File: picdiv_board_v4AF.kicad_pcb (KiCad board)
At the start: 2 copper layers, 75 x 100 mm, 83 parts, among them J1 DC-Input, J10 PPS_B, J11 PPS_B, J2 MountingHole_M2.5, J3 MountingHole_M2.5, J4 TEST_1PPS, J5 Conn_01x06, J8 PPS_A, J9 PPS_A, SW1 SW_DIP_x03, U1 LT1963AxST-3.3, U2 LT1963AxST-3.3, U3 PIC12F675-xSN, U4 LTC6993xS6-1, U5 IDT5PB1108, U6 IDT5PB1108, U7 LT1963AEQ, U8 ADR4540

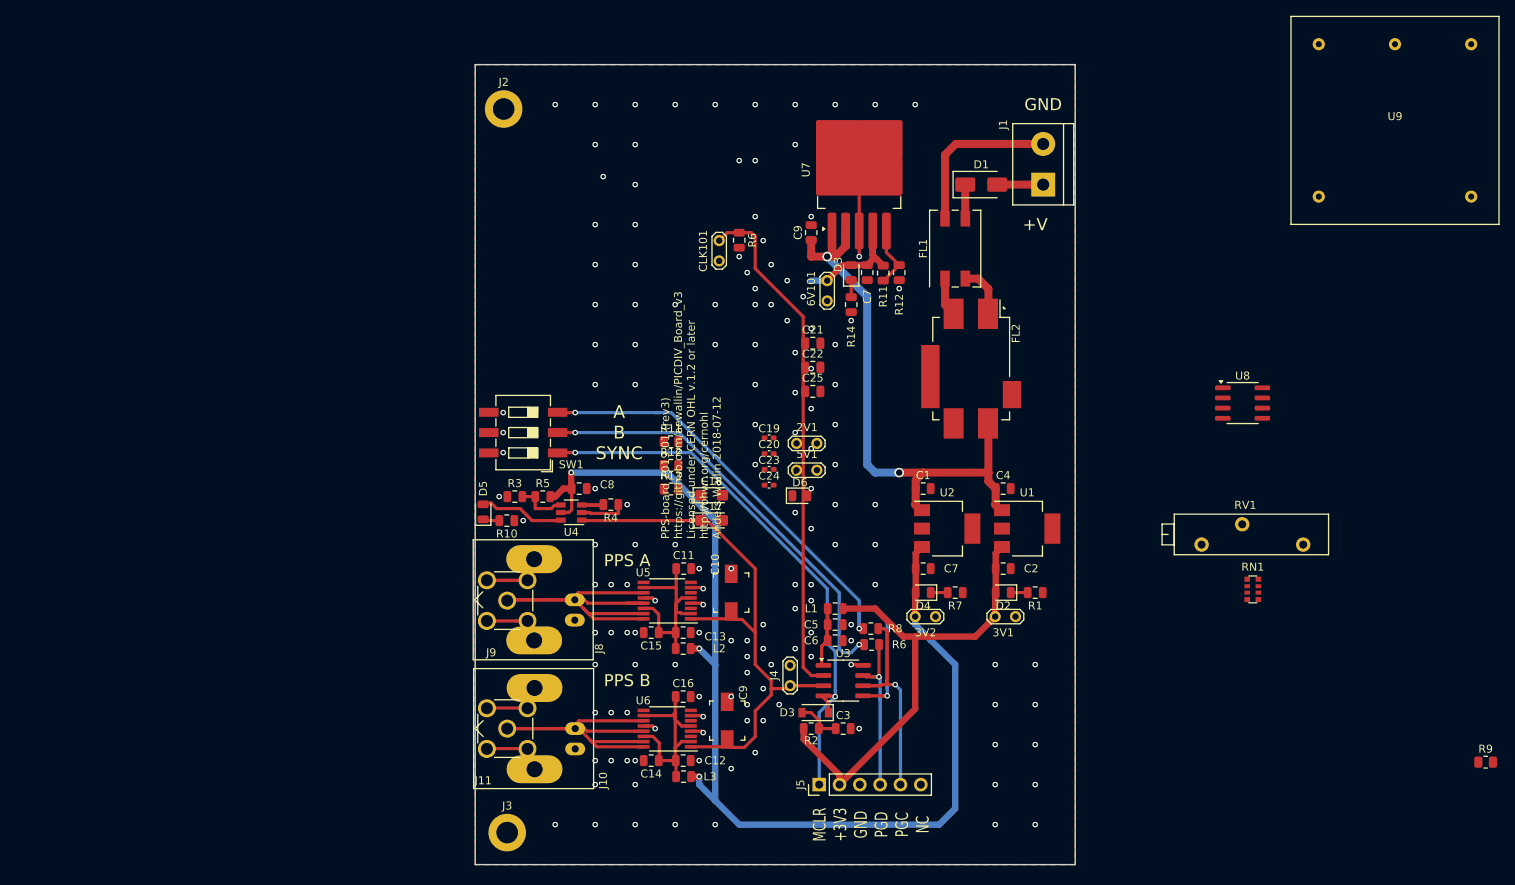
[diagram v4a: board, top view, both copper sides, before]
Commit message: Getting closer on parts placement.
Fixed a few backwards parts caused by newer libraries.  Several are mirrors of what was in the orginal symbol.  I wonder if he made his own to make the schematic clearer.
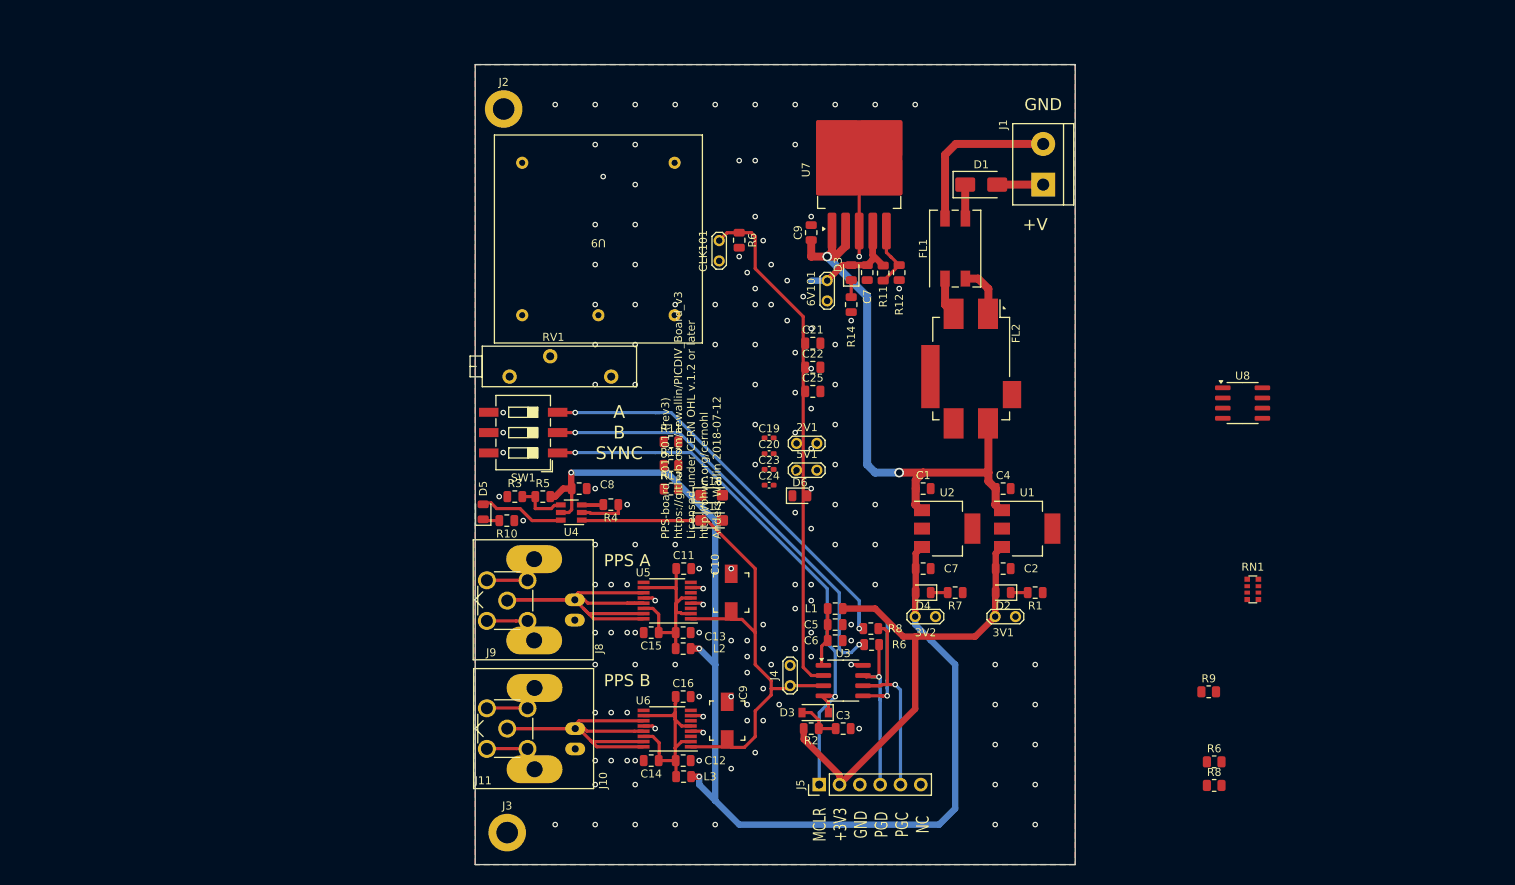
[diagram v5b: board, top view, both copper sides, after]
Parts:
- added R6: 10k, Resistor_SMD:R_0805_2012Metric, F.Cu at (217.4, 137.2)
- added R8: 10k, Resistor_SMD:R_0805_2012Metric, F.Cu at (217.4, 140.1)
- moved U9 100.7 mm to (140.4, 71.8), turned to 180 degrees
- moved RV1 89.0 mm to (142.0, 89.0)
- moved R9 35.7 mm to (216.7, 128.4)
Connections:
- U3 pad 2: /sync -> 10MHz
- U3 pad 3: PGC -> PPS
- U3 pad 4: PGD -> MCLR
- U3 pad 5: 10MHz -> /sync
- U3 pad 6: PPS -> PGC
- U3 pad 7: MCLR -> PGD
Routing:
- net 10MHz: track 13.5 -> 0.00 mm, vias 1 -> 0
- net /sync: track 0.00 -> 13.5 mm, vias 0 -> 1
- net Net-(RN1-R2.2): vias 0 -> 1
- net GND: vias 148 -> 147

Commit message: More layout work
99.5x100 mm board.
Sync back on the schematic.
Move some parts to make room for OCXO
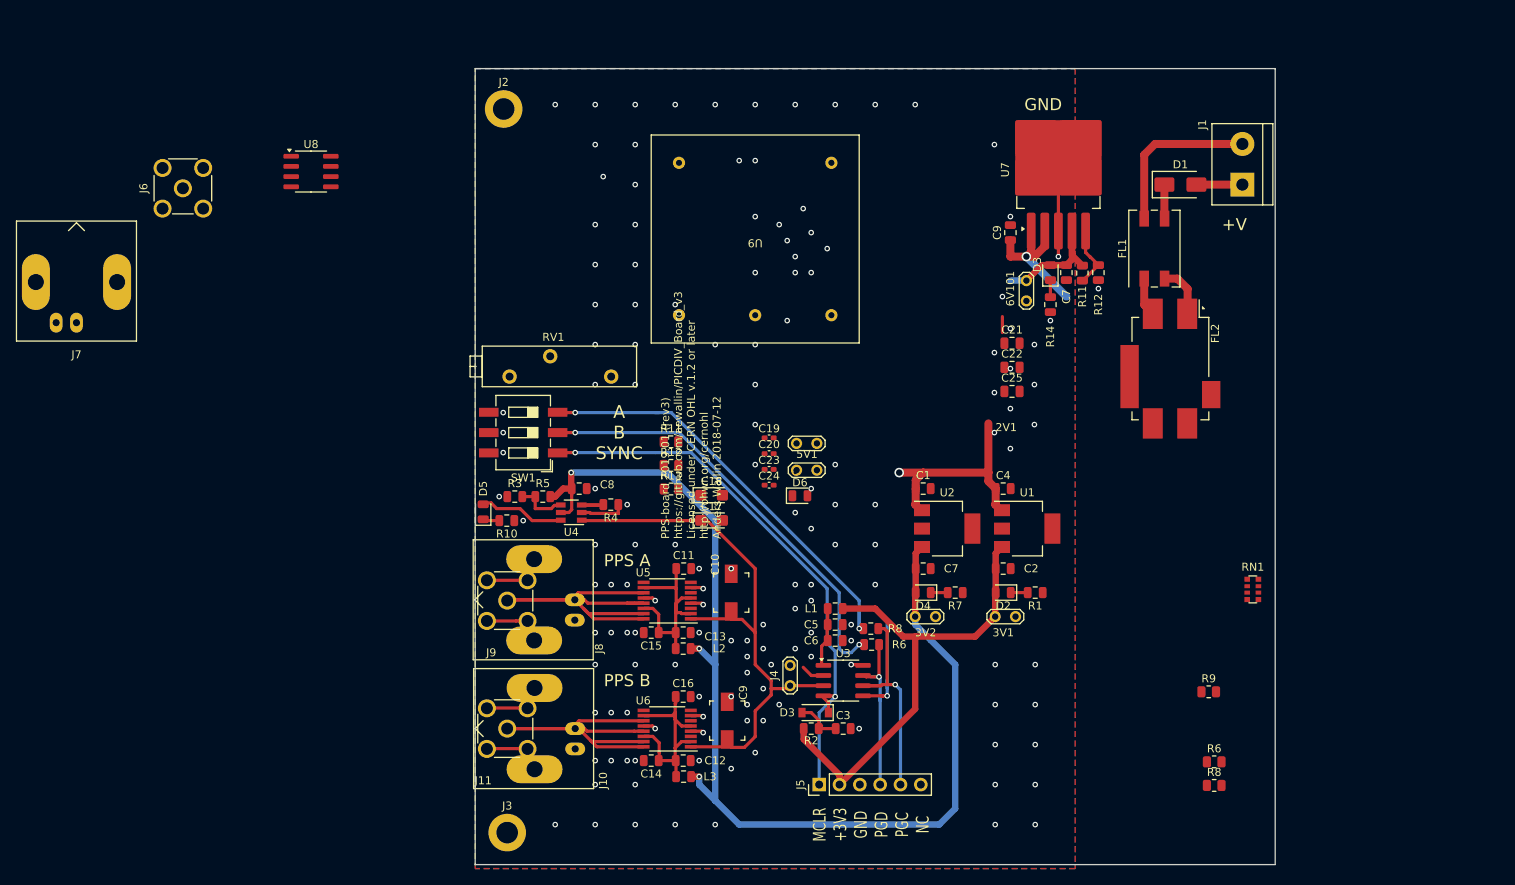
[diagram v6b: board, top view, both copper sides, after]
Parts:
- removed CLK101: TEST_CLK, TestPoint:TestPoint_2Pads_Pitch2.54mm_Drill0.8mm
- removed the R6 at (158.0, 72.0)
- added J6: Sync, Connector_Coaxial:SMA_Molex_73251-2200_Horizontal, F.Cu at (88.5, 65.5)
- added J7: Sync, Connector_Coaxial:BNC_Amphenol_B6252HB-NPP3G-50_Horizontal, F.Cu at (75.2, 82.3)
- C8: value C -> 100nF
- J8, J9: value PPS_A -> 10MHz
- moved U8 120.0 mm to (104.5, 63.4)
- moved 6V101 24.9 mm to (193.9, 77.0)
- moved C21 24.9 mm to (192.1, 84.8)
- moved C22 24.9 mm to (192.1, 87.8)
- moved C25 24.9 mm to (192.1, 90.8)
- moved C7 24.9 mm to (198.9, 76.0)
- moved C9 24.9 mm to (191.9, 71.0)
- moved D1 24.9 mm to (213.2, 65.0)
- moved D3 24.9 mm to (196.9, 76.0)
- moved FL1 24.9 mm to (209.9, 73.0)
- moved FL2 24.9 mm to (211.9, 88.0)
- moved J1 24.9 mm to (220.9, 65.0)
- moved R11 24.9 mm to (200.9, 76.1)
- moved R12 24.9 mm to (202.9, 76.0)
- moved R14 24.9 mm to (196.9, 80.0)
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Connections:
- C9 pad 2: PPS -> 10MHz
- R9 pad 2: GND -> Net-(J6-In)
- U5 pad 1: PPS -> 10MHz
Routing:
- net CLK: track 64.2 -> 0.00 mm
- net LDO_IN: track 73.2 -> 47.8 mm, vias 2 -> 3
- net 10MHz: track 0.00 -> 2.72 mm
- net (no net): track 0.00 -> 2.00 mm
- net Net-(RN1-R1.2): vias 1 -> 2
- net GND: vias 147 -> 143
- net +5V: vias 1 -> 3
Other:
- board size 75 x 100 mm -> 100 x 99.5 mm
- board text removed: "multi-cb pricing as of 2018-08 75x100, 2-sided, ENIG, top-silk ca 24eur/pcs for two"

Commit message: More Layout work
All parts are "on the board".    Added some missing LCSC part numbers.  Fixed a few "lost parts" that happened when I updated the original schematic to the current version of KiCad.
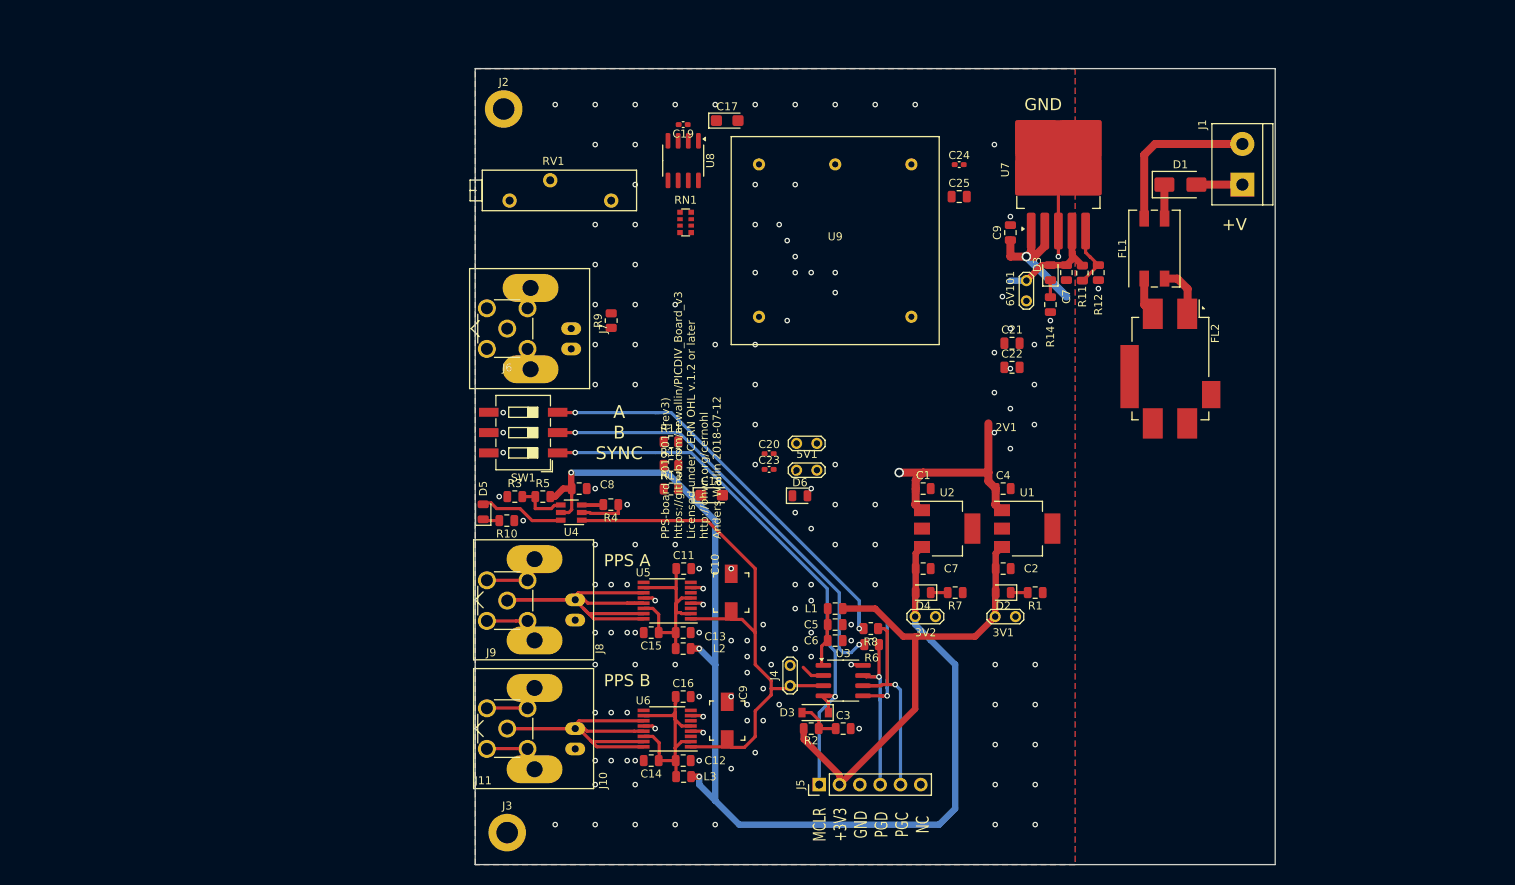
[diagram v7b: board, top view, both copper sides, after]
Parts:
- removed the R6 at (174.6, 122.5)
- removed the R8 at (174.4, 120.5)
- moved R9 87.9 mm to (142.0, 82.0), turned to 90 degrees
- moved RN1 84.4 mm to (151.3, 69.7)
- moved J7 61.8 mm to (137.0, 83.0), turned to 90 degrees
- moved C17 50.0 mm to (156.5, 57.0)
- moved R8 47.2 mm to (174.4, 120.5), turned to 180 degrees
- moved C24 46.6 mm to (185.5, 62.5)
- moved U8 46.5 mm to (151.0, 62.0), turned to -90 degrees
- moved R6 45.3 mm to (174.6, 122.5), turned to 180 degrees
- moved J6 44.2 mm to (129.0, 83.0), turned to 90 degrees
- moved C19 40.6 mm to (151.0, 57.5), turned to 180 degrees
- moved C25 25.2 mm to (185.5, 66.5)
- moved RV1 22.0 mm to (142.0, 67.0)
- moved U9 10.0 mm to (170.0, 72.0), turned to 0 degrees
- moved J8 0.05 mm to (137.5, 116.9)
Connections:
- net /PPS_A renamed Net-(J8-In)
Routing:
- net (no net): track 2.00 -> 0.00 mm
- net GND: vias 143 -> 141
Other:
- board text added: "10MHz output"
- board text added: "PPS output"
- board text removed: "PPS A output"
- board text removed: "PPS B output"

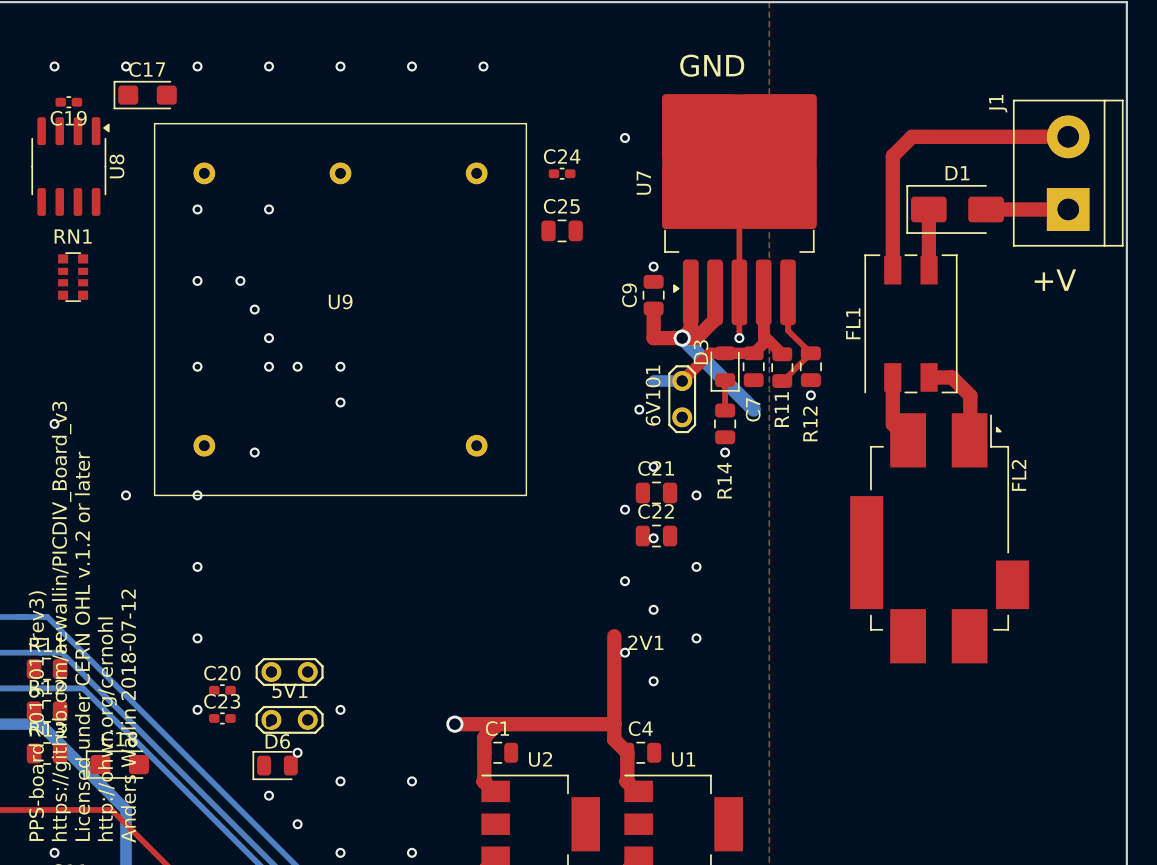
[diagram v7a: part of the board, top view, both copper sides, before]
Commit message: Add .stp file for FL1
Added manufacturer .stp file for FL1.   The footprint is a kicad library part, so I made the change on the schematic.
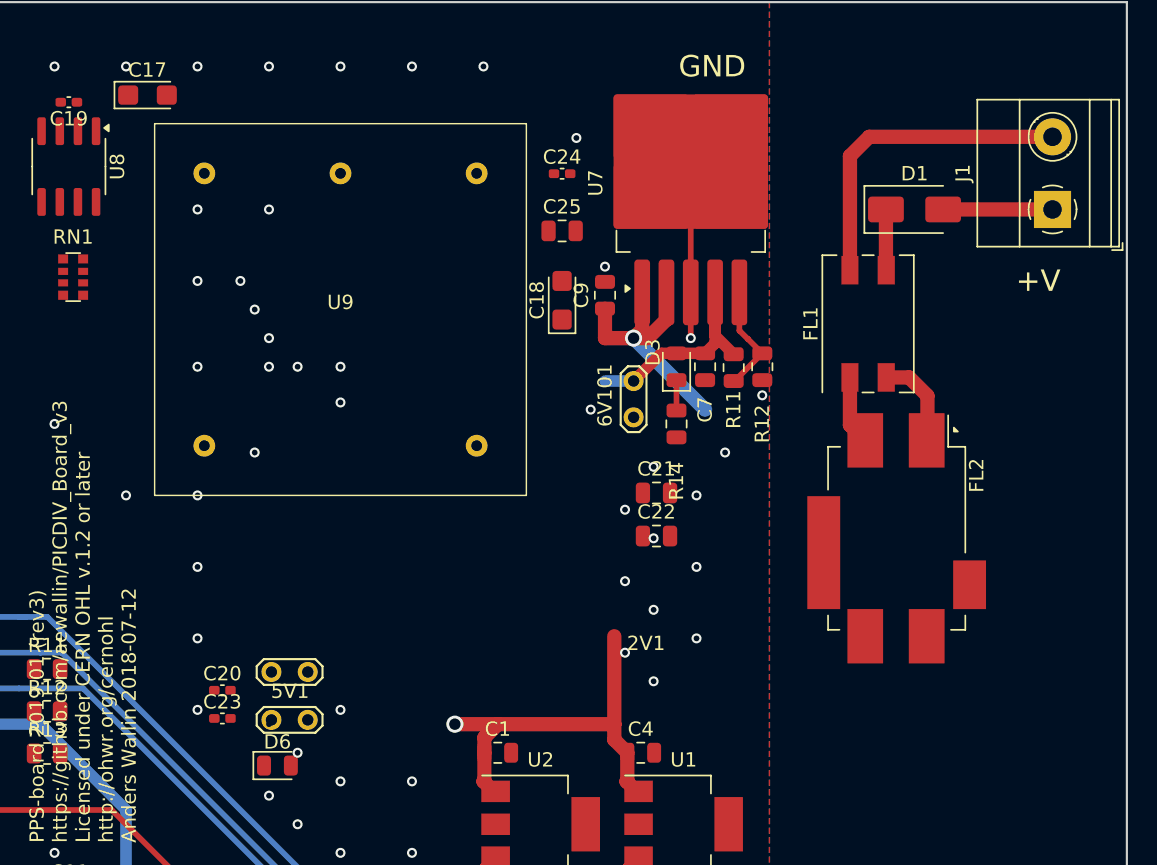
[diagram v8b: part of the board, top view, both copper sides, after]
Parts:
- J1: footprint Connectors_Terminal_Blocks:TerminalBlock_bornier-2_P5.08mm -> TerminalBlock_Phoenix:TerminalBlock_Phoenix_MKDS-1,5-2-5.08_1x02_P5.08mm_Horizontal
- moved C18 44.9 mm to (185.5, 71.3), turned to 90 degrees
- moved 6V101 3.40 mm to (190.5, 77.0)
- moved C7 3.40 mm to (195.5, 76.0)
- moved C9 3.40 mm to (188.5, 71.0)
- moved D3 3.40 mm to (193.5, 76.0)
- moved R11 3.40 mm to (197.5, 76.1)
- moved R12 3.40 mm to (199.5, 76.0)
- moved R14 3.40 mm to (193.5, 80.0)
- moved U7 3.40 mm to (194.5, 63.1)
- moved D1 3.00 mm to (210.2, 65.0)
- moved FL1 3.00 mm to (206.9, 73.0)
- moved FL2 3.00 mm to (208.9, 88.0)
- moved J1 1.10 mm to (219.8, 65.0)
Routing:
- net /w4: track 20.8 -> 22.7 mm
- net /w1: track 5.75 -> 7.65 mm
